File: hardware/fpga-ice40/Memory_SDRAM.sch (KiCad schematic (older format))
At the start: 8 parts, among them U2 IS42S16320F-6TL

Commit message: Reannotate schematic symbols
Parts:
- renumbered C18 to C10, C19 to C11, C20 to C12, C21 to C13, C15 to C7, C16 to C8, C17 to C9, U2 to U4
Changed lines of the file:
@@
 P 6900 3300
 AR Path="/5F8AF4C4" Ref="C?"  Part="1"
-AR Path="/5F892E2D/5F8AF4C4" Ref="C15"  Part="1"
-F 0 "C15" H 6950 3400 50  0000 L CNN
+AR Path="/5F892E2D/5F8AF4C4" Ref="C7"  Part="1"
+F 0 "C7" H 6950 3400 50  0000 L CNN
 F 1 "100n" H 6950 3200 50  0000 L CNN
 F 2 "Capacitor_SMD:C_0603_1608Metric" H 6938 3150 50  0001 C CNN
@@
 P 7200 3300
 AR Path="/5F8AF4CA" Ref="C?"  Part="1"
-AR Path="/5F892E2D/5F8AF4CA" Ref="C16"  Part="1"
-F 0 "C16" H 7250 3400 50  0000 L CNN
+AR Path="/5F892E2D/5F8AF4CA" Ref="C8"  Part="1"
+F 0 "C8" H 7250 3400 50  0000 L CNN
 F 1 "100n" H 7250 3200 50  0000 L CNN
 F 2 "Capacitor_SMD:C_0603_1608Metric" H 7238 3150 50  0001 C CNN
@@
 P 7500 3300
 AR Path="/5F8AF4D0" Ref="C?"  Part="1"
-AR Path="/5F892E2D/5F8AF4D0" Ref="C17"  Part="1"
-F 0 "C17" H 7550 3400 50  0000 L CNN
+AR Path="/5F892E2D/5F8AF4D0" Ref="C9"  Part="1"
+F 0 "C9" H 7550 3400 50  0000 L CNN
 F 1 "100n" H 7550 3200 50  0000 L CNN
 F 2 "Capacitor_SMD:C_0603_1608Metric" H 7538 3150 50  0001 C CNN
@@
 P 6900 4650
 AR Path="/5F8AF4D6" Ref="C?"  Part="1"
-AR Path="/5F892E2D/5F8AF4D6" Ref="C18"  Part="1"
-F 0 "C18" H 6950 4750 50  0000 L CNN
+AR Path="/5F892E2D/5F8AF4D6" Ref="C10"  Part="1"
+F 0 "C10" H 6950 4750 50  0000 L CNN
 F 1 "100n" H 6950 4550 50  0000 L CNN
 F 2 "Capacitor_SMD:C_0603_1608Metric" H 6938 4500 50  0001 C CNN
@@
 P 7200 4650
 AR Path="/5F8AF4DC" Ref="C?"  Part="1"
-AR Path="/5F892E2D/5F8AF4DC" Ref="C19"  Part="1"
-F 0 "C19" H 7250 4750 50  0000 L CNN
+AR Path="/5F892E2D/5F8AF4DC" Ref="C11"  Part="1"
+F 0 "C11" H 7250 4750 50  0000 L CNN
 F 1 "100n" H 7250 4550 50  0000 L CNN
 F 2 "Capacitor_SMD:C_0603_1608Metric" H 7238 4500 50  0001 C CNN
@@
 P 7500 4650
 AR Path="/5F8AF4E2" Ref="C?"  Part="1"
-AR Path="/5F892E2D/5F8AF4E2" Ref="C20"  Part="1"
-F 0 "C20" H 7550 4750 50  0000 L CNN
+AR Path="/5F892E2D/5F8AF4E2" Ref="C12"  Part="1"
+F 0 "C12" H 7550 4750 50  0000 L CNN
 F 1 "100n" H 7550 4550 50  0000 L CNN
 F 2 "Capacitor_SMD:C_0603_1608Metric" H 7538 4500 50  0001 C CNN
@@
 P 7800 4650
 AR Path="/5F8AF4E8" Ref="C?"  Part="1"
-AR Path="/5F892E2D/5F8AF4E8" Ref="C21"  Part="1"
-F 0 "C21" H 7850 4750 50  0000 L CNN
+AR Path="/5F892E2D/5F8AF4E8" Ref="C13"  Part="1"
+F 0 "C13" H 7850 4750 50  0000 L CNN
 F 1 "100n" H 7850 4550 50  0000 L CNN
 F 2 "Capacitor_SMD:C_0603_1608Metric" H 7838 4500 50  0001 C CNN
@@
 P 4600 3900
 AR Path="/5F8AF513" Ref="U?"  Part="1"
-AR Path="/5F892E2D/5F8AF513" Ref="U2"  Part="1"
-F 0 "U2" H 5050 5250 50  0000 L CNN
+AR Path="/5F892E2D/5F8AF513" Ref="U4"  Part="1"
+F 0 "U4" H 5050 5250 50  0000 L CNN
 F 1 "IS42S16320F-6TL" H 5050 5150 50  0000 L CNN
 F 2 "Package_SO:TSOP-II-54_22.2x10.16mm_P0.8mm" H 4700 4300 50  0001 C CNN
@@
 P 4250 5900
 AR Path="/5F8AF544" Ref="#PWR?"  Part="1"
-AR Path="/5F892E2D/5F8AF544" Ref="#PWR0109"  Part="1"
-F 0 "#PWR0109" H 4250 5650 50  0001 C CNN
+AR Path="/5F892E2D/5F8AF544" Ref="#PWR011"  Part="1"
+F 0 "#PWR011" H 4250 5650 50  0001 C CNN
 F 1 "GND" H 4253 5774 50  0000 C CNN
 F 2 "" H 4150 5550 50  0001 C CNN
@@
 P 6900 3650
 AR Path="/5F8AF54B" Ref="#PWR?"  Part="1"
-AR Path="/5F892E2D/5F8AF54B" Ref="#PWR0110"  Part="1"
-F 0 "#PWR0110" H 6900 3400 50  0001 C CNN
+AR Path="/5F892E2D/5F8AF54B" Ref="#PWR09"  Part="1"
+F 0 "#PWR09" H 6900 3400 50  0001 C CNN
 F 1 "GND" H 6903 3524 50  0000 C CNN
 F 2 "" H 6800 3300 50  0001 C CNN
@@
 P 6900 5000
 AR Path="/5F8AF551" Ref="#PWR?"  Part="1"
-AR Path="/5F892E2D/5F8AF551" Ref="#PWR0111"  Part="1"
-F 0 "#PWR0111" H 6900 4750 50  0001 C CNN
+AR Path="/5F892E2D/5F8AF551" Ref="#PWR010"  Part="1"
+F 0 "#PWR010" H 6900 4750 50  0001 C CNN
 F 1 "GND" H 6903 4874 50  0000 C CNN
 F 2 "" H 6800 4650 50  0001 C CNN

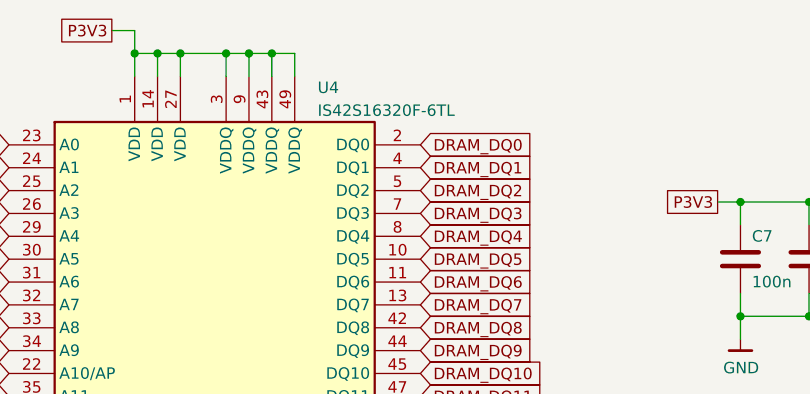
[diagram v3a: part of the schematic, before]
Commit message: Component selection by MPN and routing cleanup
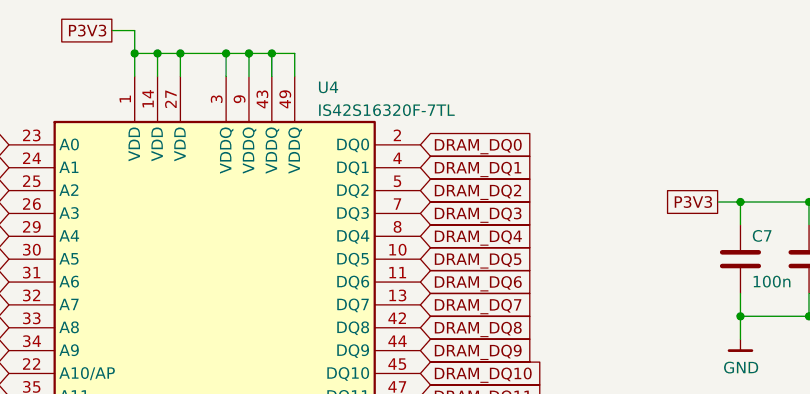
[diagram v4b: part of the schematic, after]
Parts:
- C10, C11, C12, C13, C7, C8, C9: MPN (none) -> CL10B104KB8NNNC
- U4: value IS42S16320F-6TL -> IS42S16320F-7TL; MPN (none) -> IS42S16320F-7TL
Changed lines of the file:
@@
 F 2 "Capacitor_SMD:C_0603_1608Metric" H 6938 3150 50  0001 C CNN
 F 3 "~" H 6900 3300 50  0001 C CNN
+F 4 "CL10B104KB8NNNC" H 6900 3300 50  0001 C CNN "MPN"
 	1    6900 3300
 	1    0    0    -1
@@
 F 2 "Capacitor_SMD:C_0603_1608Metric" H 7238 3150 50  0001 C CNN
 F 3 "~" H 7200 3300 50  0001 C CNN
+F 4 "CL10B104KB8NNNC" H 7200 3300 50  0001 C CNN "MPN"
 	1    7200 3300
 	1    0    0    -1
@@
 F 2 "Capacitor_SMD:C_0603_1608Metric" H 7538 3150 50  0001 C CNN
 F 3 "~" H 7500 3300 50  0001 C CNN
+F 4 "CL10B104KB8NNNC" H 7500 3300 50  0001 C CNN "MPN"
 	1    7500 3300
 	1    0    0    -1
@@
 F 2 "Capacitor_SMD:C_0603_1608Metric" H 6938 4500 50  0001 C CNN
 F 3 "~" H 6900 4650 50  0001 C CNN
+F 4 "CL10B104KB8NNNC" H 6900 4650 50  0001 C CNN "MPN"
 	1    6900 4650
 	1    0    0    -1
@@
 F 2 "Capacitor_SMD:C_0603_1608Metric" H 7238 4500 50  0001 C CNN
 F 3 "~" H 7200 4650 50  0001 C CNN
+F 4 "CL10B104KB8NNNC" H 7200 4650 50  0001 C CNN "MPN"
 	1    7200 4650
 	1    0    0    -1
@@
 F 2 "Capacitor_SMD:C_0603_1608Metric" H 7538 4500 50  0001 C CNN
 F 3 "~" H 7500 4650 50  0001 C CNN
+F 4 "CL10B104KB8NNNC" H 7500 4650 50  0001 C CNN "MPN"
 	1    7500 4650
 	1    0    0    -1
@@
 F 2 "Capacitor_SMD:C_0603_1608Metric" H 7838 4500 50  0001 C CNN
 F 3 "~" H 7800 4650 50  0001 C CNN
+F 4 "CL10B104KB8NNNC" H 7800 4650 50  0001 C CNN "MPN"
 	1    7800 4650
 	1    0    0    -1
@@
 AR Path="/5F892E2D/5F8AF513" Ref="U4"  Part="1"
 F 0 "U4" H 5050 5250 50  0000 L CNN
-F 1 "IS42S16320F-6TL" H 5050 5150 50  0000 L CNN
+F 1 "IS42S16320F-7TL" H 5050 5150 50  0000 L CNN
 F 2 "Package_SO:TSOP-II-54_22.2x10.16mm_P0.8mm" H 4700 4300 50  0001 C CNN
 F 3 "https://www.mouser.com/datasheet/2/198/42-45R-S_86400F-16320F-706495.pdf" H 4000 5150 50  0001 C CNN
+F 4 "IS42S16320F-7TL" H 4600 3900 50  0001 C CNN "MPN"
 	1    4600 3900
 	1    0    0    -1

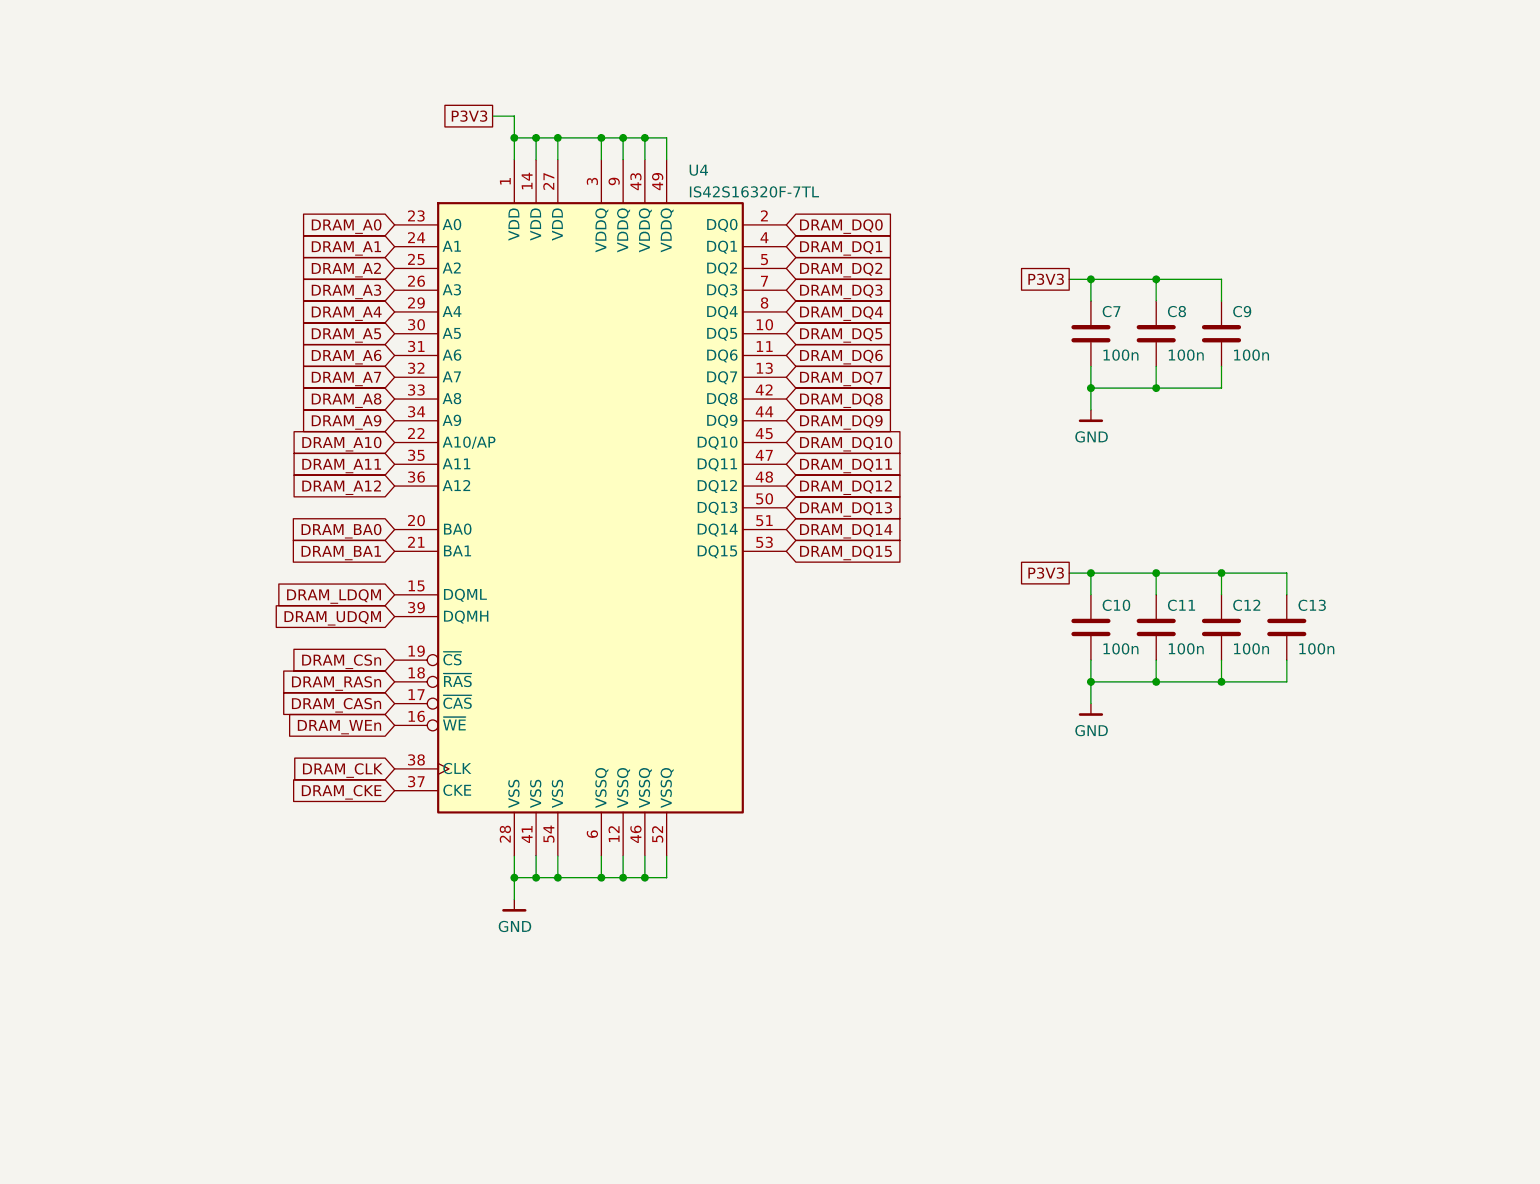
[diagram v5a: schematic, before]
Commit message: Add series termination resistors to SDRAM bus
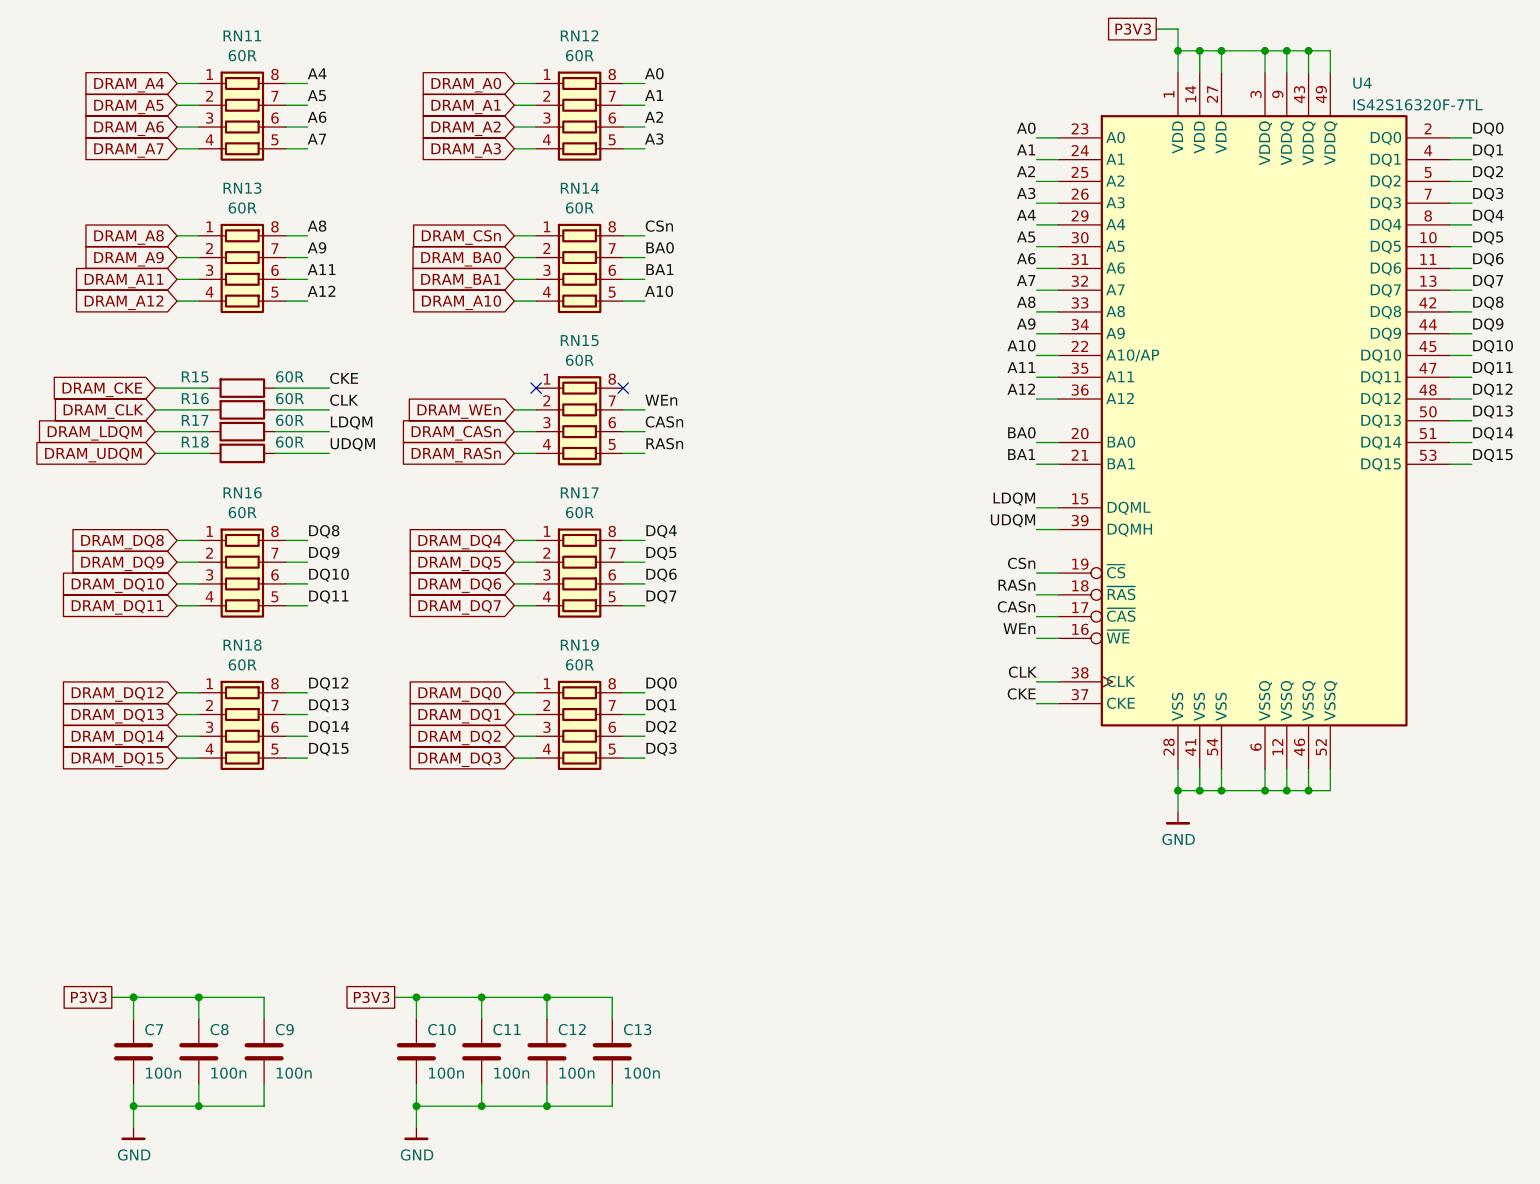
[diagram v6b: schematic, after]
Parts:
- added R15, R16, R17, R18: 60R, Resistor_SMD:R_0603_1608Metric, symbol Device:R
- added RN11, RN12, RN13, RN14, RN15, RN16, RN17, RN18, RN19: 60R, Resistor_SMD:R_Array_Convex_4x0603, symbol Device:R_Pack04
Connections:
- net DRAM_A0: now also RN12.1 (R1.1); no longer U4.23 (A0)
- net DRAM_A1: now also RN12.2 (R2.1); no longer U4.24 (A1)
- net DRAM_A10: now also RN14.4 (R4.1); no longer U4.22 (A10/AP)
- net DRAM_A11: now also RN13.3 (R3.1); no longer U4.35 (A11)
- net DRAM_A12: now also RN13.4 (R4.1); no longer U4.36 (A12)
- net DRAM_A2: now also RN12.3 (R3.1); no longer U4.25 (A2)
- net DRAM_A3: now also RN12.4 (R4.1); no longer U4.26 (A3)
- net DRAM_A4: now also RN11.1 (R1.1); no longer U4.29 (A4)
- net DRAM_A5: now also RN11.2 (R2.1); no longer U4.30 (A5)
- net DRAM_A6: now also RN11.3 (R3.1); no longer U4.31 (A6)
- net DRAM_A7: now also RN11.4 (R4.1); no longer U4.32 (A7)
- net DRAM_A8: now also RN13.1 (R1.1); no longer U4.33 (A8)
- net DRAM_A9: now also RN13.2 (R2.1); no longer U4.34 (A9)
- net DRAM_BA0: now also RN14.2 (R2.1); no longer U4.20 (BA0)
- net DRAM_BA1: now also RN14.3 (R3.1); no longer U4.21 (BA1)
- net DRAM_CASn: now also RN15.3 (R3.1); no longer U4.17 (~CAS)
- net DRAM_CKE: now also R15.2; no longer U4.37 (CKE)
- net DRAM_CLK: now also R16.2; no longer U4.38 (CLK)
- net DRAM_CSn: now also RN14.1 (R1.1); no longer U4.19 (~CS)
- net DRAM_DQ0: now also RN19.1 (R1.1); no longer U4.2 (DQ0)
- net DRAM_DQ1: now also RN19.2 (R2.1); no longer U4.4 (DQ1)
- net DRAM_DQ10: now also RN16.3 (R3.1); no longer U4.45 (DQ10)
- net DRAM_DQ11: now also RN16.4 (R4.1); no longer U4.47 (DQ11)
- net DRAM_DQ12: now also RN18.1 (R1.1); no longer U4.48 (DQ12)
- net DRAM_DQ13: now also RN18.2 (R2.1); no longer U4.50 (DQ13)
- net DRAM_DQ14: now also RN18.3 (R3.1); no longer U4.51 (DQ14)
- net DRAM_DQ15: now also RN18.4 (R4.1); no longer U4.53 (DQ15)
- net DRAM_DQ2: now also RN19.3 (R3.1); no longer U4.5 (DQ2)
- net DRAM_DQ3: now also RN19.4 (R4.1); no longer U4.7 (DQ3)
- net DRAM_DQ4: now also RN17.1 (R1.1); no longer U4.8 (DQ4)
- net DRAM_DQ5: now also RN17.2 (R2.1); no longer U4.10 (DQ5)
- net DRAM_DQ6: now also RN17.3 (R3.1); no longer U4.11 (DQ6)
- net DRAM_DQ7: now also RN17.4 (R4.1); no longer U4.13 (DQ7)
- net DRAM_DQ8: now also RN16.1 (R1.1); no longer U4.42 (DQ8)
- net DRAM_DQ9: now also RN16.2 (R2.1); no longer U4.44 (DQ9)
- net DRAM_LDQM: now also R17.2; no longer U4.15 (DQML)
- net DRAM_RASn: now also RN15.4 (R4.1); no longer U4.18 (~RAS)
- net DRAM_UDQM: now also R18.2; no longer U4.39 (DQMH)
- net DRAM_WEn: now also RN15.2 (R2.1); no longer U4.16 (~WE)
- new net A0: RN12.8 (R1.2), U4.23 (A0)
- new net A1: RN12.7 (R2.2), U4.24 (A1)
- new net A10: RN14.5 (R4.2), U4.22 (A10/AP)
- new net A11: RN13.6 (R3.2), U4.35 (A11)
- new net A12: RN13.5 (R4.2), U4.36 (A12)
- new net A2: RN12.6 (R3.2), U4.25 (A2)
- new net A3: RN12.5 (R4.2), U4.26 (A3)
- new net A4: RN11.8 (R1.2), U4.29 (A4)
- new net A5: RN11.7 (R2.2), U4.30 (A5)
- new net A6: RN11.6 (R3.2), U4.31 (A6)
- new net A7: RN11.5 (R4.2), U4.32 (A7)
- new net A8: RN13.8 (R1.2), U4.33 (A8)
- new net A9: RN13.7 (R2.2), U4.34 (A9)
- new net BA0: RN14.7 (R2.2), U4.20 (BA0)
- new net BA1: RN14.6 (R3.2), U4.21 (BA1)
- new net CASn: RN15.6 (R3.2), U4.17 (~CAS)
- new net CKE: R15.1, U4.37 (CKE)
- new net CLK: R16.1, U4.38 (CLK)
- new net CSn: RN14.8 (R1.2), U4.19 (~CS)
- new net DQ0: RN19.8 (R1.2), U4.2 (DQ0)
- new net DQ1: RN19.7 (R2.2), U4.4 (DQ1)
- new net DQ10: RN16.6 (R3.2), U4.45 (DQ10)
- new net DQ11: RN16.5 (R4.2), U4.47 (DQ11)
- new net DQ12: RN18.8 (R1.2), U4.48 (DQ12)
- new net DQ13: RN18.7 (R2.2), U4.50 (DQ13)
- new net DQ14: RN18.6 (R3.2), U4.51 (DQ14)
- new net DQ15: RN18.5 (R4.2), U4.53 (DQ15)
- new net DQ2: RN19.6 (R3.2), U4.5 (DQ2)
- new net DQ3: RN19.5 (R4.2), U4.7 (DQ3)
- new net DQ4: RN17.8 (R1.2), U4.8 (DQ4)
- new net DQ5: RN17.7 (R2.2), U4.10 (DQ5)
- new net DQ6: RN17.6 (R3.2), U4.11 (DQ6)
- new net DQ7: RN17.5 (R4.2), U4.13 (DQ7)
- new net DQ8: RN16.8 (R1.2), U4.42 (DQ8)
- new net DQ9: RN16.7 (R2.2), U4.44 (DQ9)
- new net LDQM: R17.1, U4.15 (DQML)
- new net RASn: RN15.5 (R4.2), U4.18 (~RAS)
- new net UDQM: R18.1, U4.39 (DQMH)
- new net WEn: RN15.7 (R2.2), U4.16 (~WE)
- no-connect marks 0 -> 2
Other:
- moved on the sheet: C10, C11, C12, C13, C7, C8, C9, U4
